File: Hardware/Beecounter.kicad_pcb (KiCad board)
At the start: 2 copper layers, 171 parts, among them J1 Conn_01x03, J10 Conn_01x03, J11 Conn_01x03, J12 Conn_01x03, J13 Conn_01x03, J14 Conn_01x03, J15 Conn_02x20_Odd_Even, J16 Conn_01x04, J17 Conn_01x10, J2 Conn_01x03, J3 Conn_01x03, J4 Conn_01x03, J5 Conn_01x03, J6 Conn_01x03, J7 Conn_01x03, J8 Conn_01x03, J9 Conn_01x03, U1 LM393, U10 LM393, U11 H2010, U12 LM393, U13 H2010, U14 LM393, U15 H2010, U16 LM393, U17 H2010, U18 LM393, U19 H2010, U2 H2010, U20 LM393, U21 H2010, U22 LM393, U23 H2010, U24 LM393, U25 H2010, U26 LM393, U27 H2010, U28 LM393, U3 H2010, U4 LM393, U5 H2010, U6 LM393, U7 H2010, U8 LM393, U9 H2010

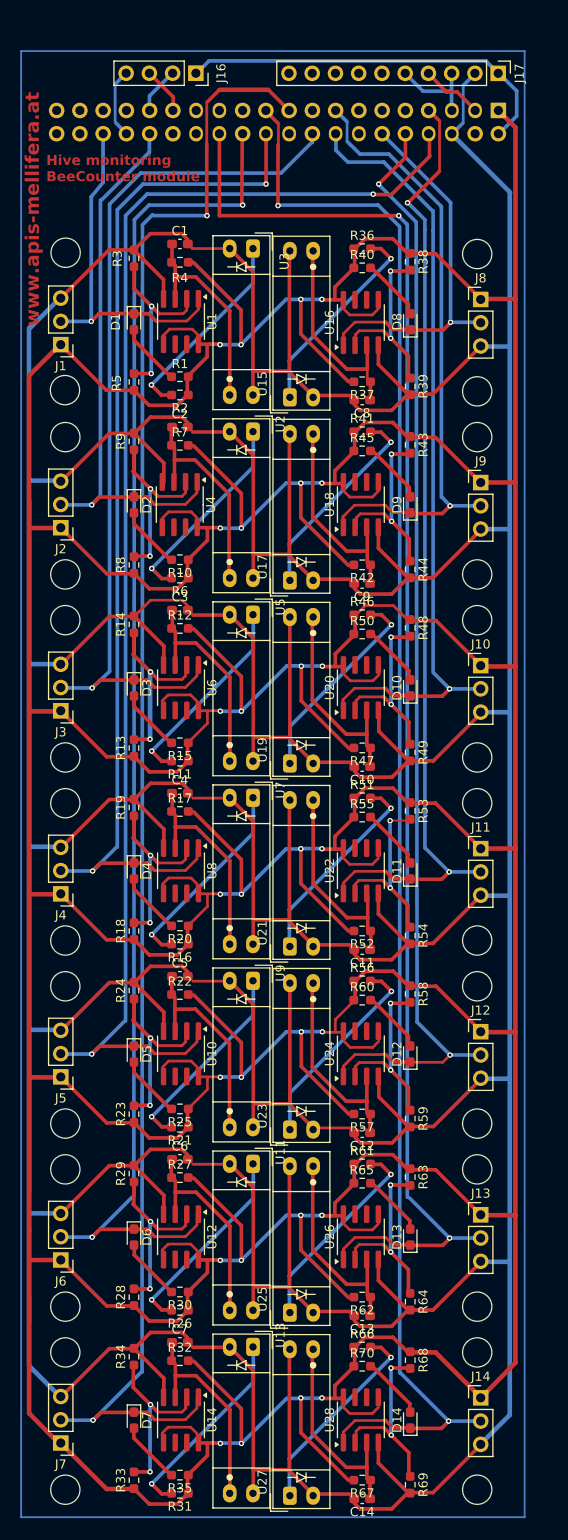
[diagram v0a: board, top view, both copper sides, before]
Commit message: Removed measurement
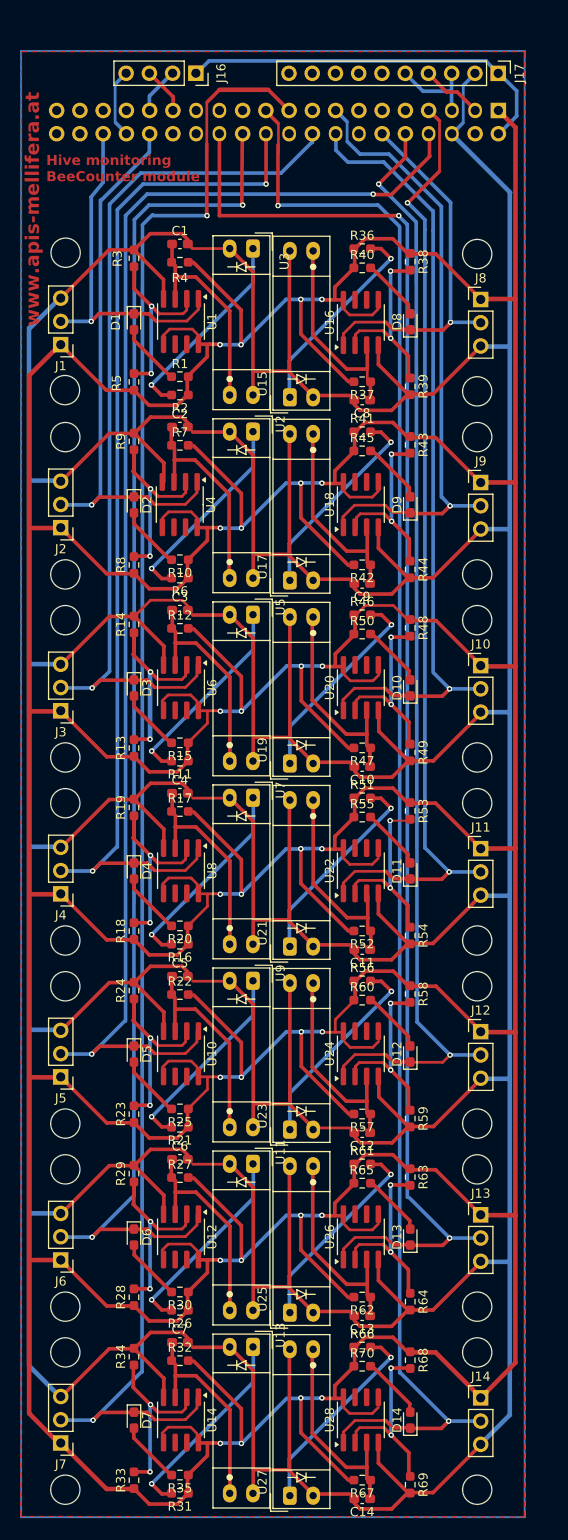
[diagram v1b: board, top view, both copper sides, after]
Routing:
- added copper zone on B.Cu, net (none)
- added copper zone on F.Cu, net GND
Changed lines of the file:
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@@
 		)
 	)
-	(dimension
-		(type aligned)
-		(layer "B.Cu")
-		(pts
-			(xy 92.99 200.39) (xy 92.99 40.39)
-		)
-		(height 7.75)
-		(gr_text "160,0000 mm"
-			(at 98.94 120.39 90)
-			(layer "B.Cu")
-			(effects
-				(font
-					(size 1.5 1.5)
-					(thickness 0.3)
-				)
-			)
-		)
-		(format
-			(prefix "")
-			(suffix "")
-			(units 3)
-			(units_format 1)
-			(precision 4)
-		)
-		(style
-			(thickness 0.2)
-			(arrow_length 1.27)
-			(text_position_mode 0)
-			(extension_height 0.58642)
-			(extension_offset 0.5) keep_text_aligned)
-	)
 	(segment
 		(start 60.5275 77.945)
@@
 		(net 114)
 	)
+	(zone
+		(net 2)
+		(net_name "GND")
+		(layer "F.Cu")
+		(name "GND F.Cu")
+		(hatch edge 0.5)
+		(priority 1)
+		(connect_pads
+			(clearance 0.5)
+		)
+		(min_thickness 0.25)
+		(filled_areas_thickness no)
+		(fill
+			(thermal_gap 0.5)
+			(thermal_bridge_width 0.5)
+		)
+		(polygon
+			(pts
+				(xy 92.77 40.43) (xy 92.75 200.52) (xy 37.71 200.47) (xy 37.78 40.43)
+			)
+		)
+	)
+	(zone
+		(net 0)
+		(net_name "")
+		(layer "B.Cu")
+		(name "GND B.Cu")
+		(hatch edge 0.5)
+		(connect_pads
+			(clearance 0.5)
+		)
+		(min_thickness 0.25)
+		(filled_areas_thickness no)
+		(fill
+			(thermal_gap 0.5)
+			(thermal_bridge_width 0.5)
+			(island_removal_mode 1)
+			(island_area_min 10)
+		)
+		(polygon
+			(pts
+				(xy 37.74 40.37) (xy 92.75 40.37) (xy 92.75 200.55) (xy 37.74 200.55)
+			)
+		)
+	)
 )

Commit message: Generated GND area and Gerber files
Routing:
- added copper zone on B.Cu, net GND
- removed copper zone on B.Cu, net (none)
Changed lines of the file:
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@@
 		(min_thickness 0.25)
 		(filled_areas_thickness no)
-		(fill
+		(fill yes
 			(thermal_gap 0.5)
 			(thermal_bridge_width 0.5)
@@
 	)
 	(zone
-		(net 0)
-		(net_name "")
+		(net 2)
+		(net_name "GND")
 		(layer "B.Cu")
 		(name "GND B.Cu")
@@
 		(min_thickness 0.25)
 		(filled_areas_thickness no)
-		(fill
+		(fill yes
 			(thermal_gap 0.5)
 			(thermal_bridge_width 0.5)

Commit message: Set origin
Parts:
- moved R56 2.31 mm to (77.2, 141.4)
- moved R60 2.31 mm to (77.2, 143.5)
- moved R61 2.31 mm to (77.2, 161.4)
- moved R65 2.31 mm to (77.2, 163.5)
- moved R66 2.31 mm to (77.2, 181.4)
- moved R70 2.31 mm to (77.2, 183.5)
- moved ? 2.31 mm to (89.8, 97.0)
- moved ? 2.31 mm to (44.8, 82.0)
- moved ? 2.31 mm to (44.8, 102.0)
- moved ? 2.31 mm to (89.8, 102.0)
- moved ? 2.31 mm to (89.8, 82.0)
- moved ? 2.31 mm to (89.8, 122.0)
- moved ? 2.31 mm to (89.8, 62.0)
- moved ? 2.31 mm to (44.8, 97.0)
- moved ? 2.31 mm to (89.8, 117.0)
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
